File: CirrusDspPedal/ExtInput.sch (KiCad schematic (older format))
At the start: 8 parts, among them J5 MonoJack2Switch, SW1 P26L-1D-RND MTL, SW2 P26L-1D-RND MTL, U6 MCP601-xOT

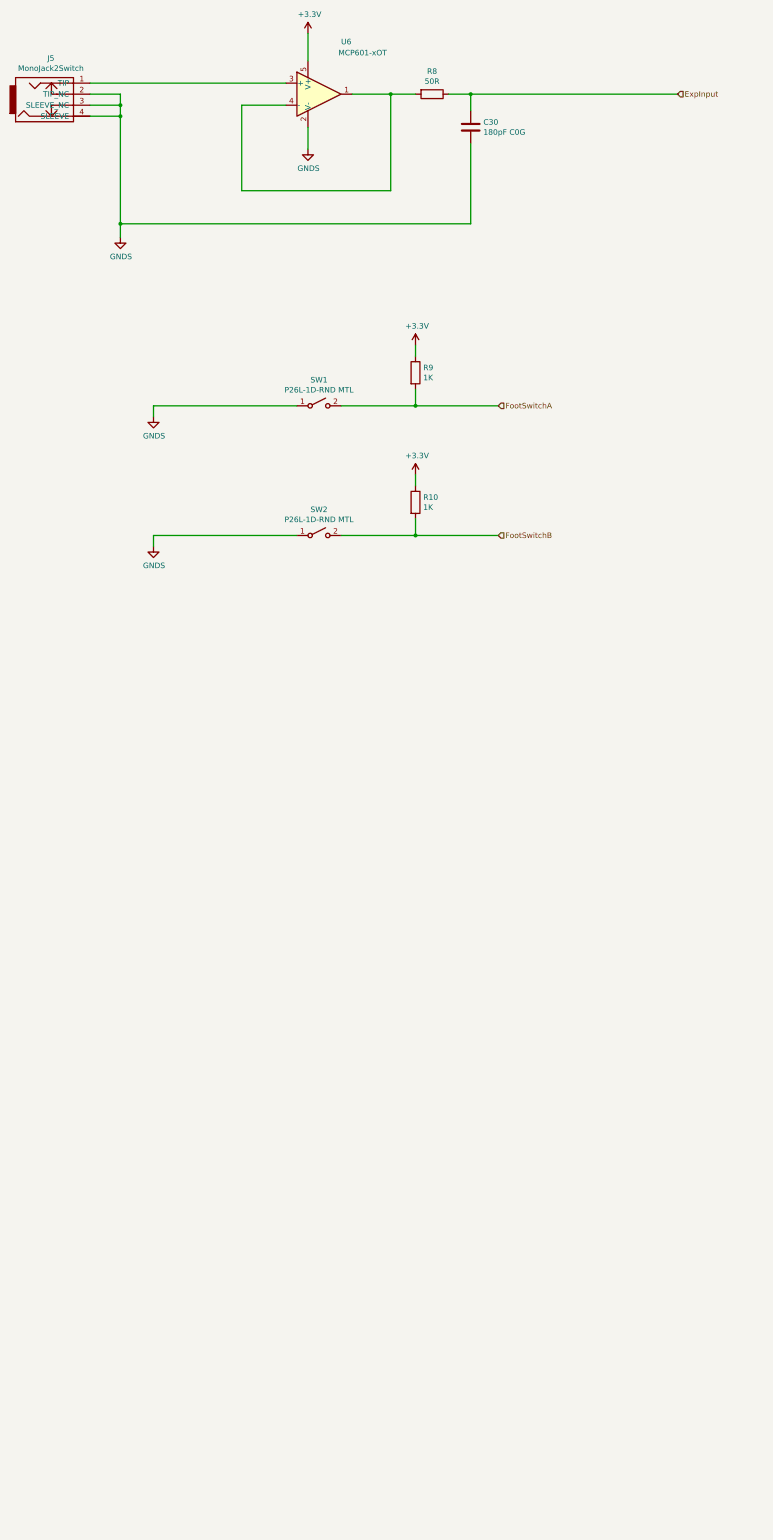
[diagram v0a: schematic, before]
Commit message: Added UserPots and RGB LEDS
Updated schema docs
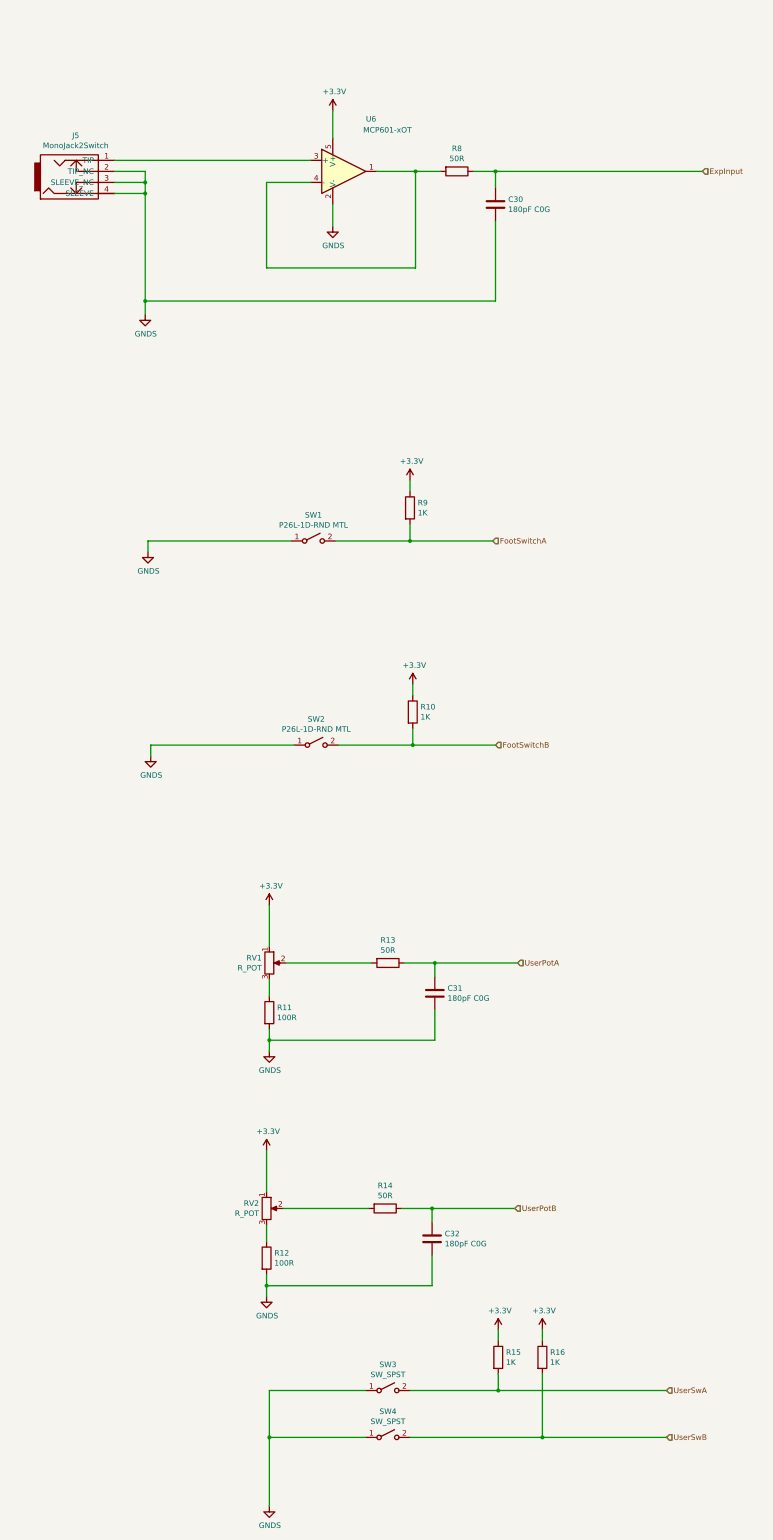
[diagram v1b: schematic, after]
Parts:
- added C31, C32: 180pF C0G, Capacitor_SMD:C_0805_2012Metric_Pad1.15x1.40mm_HandSolder, symbol Device:C
- added R11, R12: 100R, Resistor_SMD:R_0805_2012Metric_Pad1.15x1.40mm_HandSolder, symbol Device:R
- added R13, R14: 50R, Resistor_SMD:R_0805_2012Metric_Pad1.15x1.40mm_HandSolder, symbol Device:R
- added R15, R16: 1K, Resistor_SMD:R_0805_2012Metric_Pad1.15x1.40mm_HandSolder, symbol Device:R
- added RV1, RV2: R_POT, Potentiometer_THT:Potentiometer_Alps_RK09L_Single_Vertical, symbol Device:R_POT
- added SW3, SW4: SW_SPST, symbol Switch:SW_SPST
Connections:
- net +3V3: now also R15.1, R16.1, RV1.1, RV2.1
- net GNDS: now also C31.1, C32.1, R11.2, R12.2, SW3.1 (A), SW4.1 (A)
- new net: R13.2, RV1.2
- new net: R11.1, RV1.3
- new net: R14.2, RV2.2
- new net: R12.1, RV2.3
- new net UserPotA: C31.2, R13.1
- new net UserPotB: C32.2, R14.1
- new net UserSwA: R15.2, SW3.2 (B)
- new net UserSwB: R16.2, SW4.2 (B)
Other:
- moved on the sheet: C30, J5, R10, R8, R9, SW1, SW2, U6

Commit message: Completed schematic design
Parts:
- SW3, SW4: footprint (none) -> custom_sw:SW_SPDT_W6.86MM_L12.7MM_P4.8MM_D2MM
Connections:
- net ExpInput renamed FootExp_IN
- net FootSwitchA renamed FootSwitchA_IN
- net FootSwitchB renamed FootSwitchB_IN
- net UserPotA renamed UserPotA_IN
- net UserPotB renamed UserPotB_IN
- net UserSwA renamed UserSwitchA_IN
- net UserSwB renamed UserSwitchB_IN
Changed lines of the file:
@@
 $Descr A3 11693 16535 portrait
 encoding utf-8
-Sheet 9 10
+Sheet 10 11
 Title ""
 Date ""
@@
 $EndComp
 Text HLabel 8700 2400 2    50   Input ~ 0
-ExpInput
+FootExp_IN
 $Comp
 L Switch:SW_SPST SW1
@@
 	5375 5750 6050 5750
 Text HLabel 6800 5750 2    50   Input ~ 0
-FootSwitchA
+FootSwitchA_IN
 Wire Wire Line
 	6050 5750 6050 5600
@@
 	5400 7600 6075 7600
 Text HLabel 6825 7600 2    50   Input ~ 0
-FootSwitchB
+FootSwitchB_IN
 Wire Wire Line
 	6075 7600 6075 7450
@@
 	4925 9575 5700 9575
 Text HLabel 7025 9575 2    50   Input ~ 0
-UserPotA
+UserPotA_IN
 $Comp
 L Device:R R13
@@
 	4900 11800 5675 11800
 Text HLabel 7000 11800 2    50   Input ~ 0
-UserPotB
+UserPotB_IN
 $Comp
 L Device:R R14
@@
 F 0 "SW3" H 5850 13685 50  0000 C CNN
 F 1 "SW_SPST" H 5850 13594 50  0000 C CNN
-F 2 "" H 5850 13450 50  0001 C CNN
+F 2 "custom_sw:SW_SPDT_W6.86MM_L12.7MM_P4.8MM_D2MM" H 5850 13450 50  0001 C CNN
 F 3 "~" H 5850 13450 50  0001 C CNN
 	1    5850 13450
@@
 F 0 "SW4" H 5850 14110 50  0000 C CNN
 F 1 "SW_SPST" H 5850 14019 50  0000 C CNN
-F 2 "" H 5850 13875 50  0001 C CNN
+F 2 "custom_sw:SW_SPDT_W6.86MM_L12.7MM_P4.8MM_D2MM" H 5850 13875 50  0001 C CNN
 F 3 "~" H 5850 13875 50  0001 C CNN
 	1    5850 13875
@@
 $EndComp
 Text HLabel 8375 13450 2    50   Input ~ 0
-UserSwA
+UserSwitchA_IN
 Text HLabel 8375 13875 2    50   Input ~ 0
-UserSwB
+UserSwitchB_IN
 $EndSCHEMATC

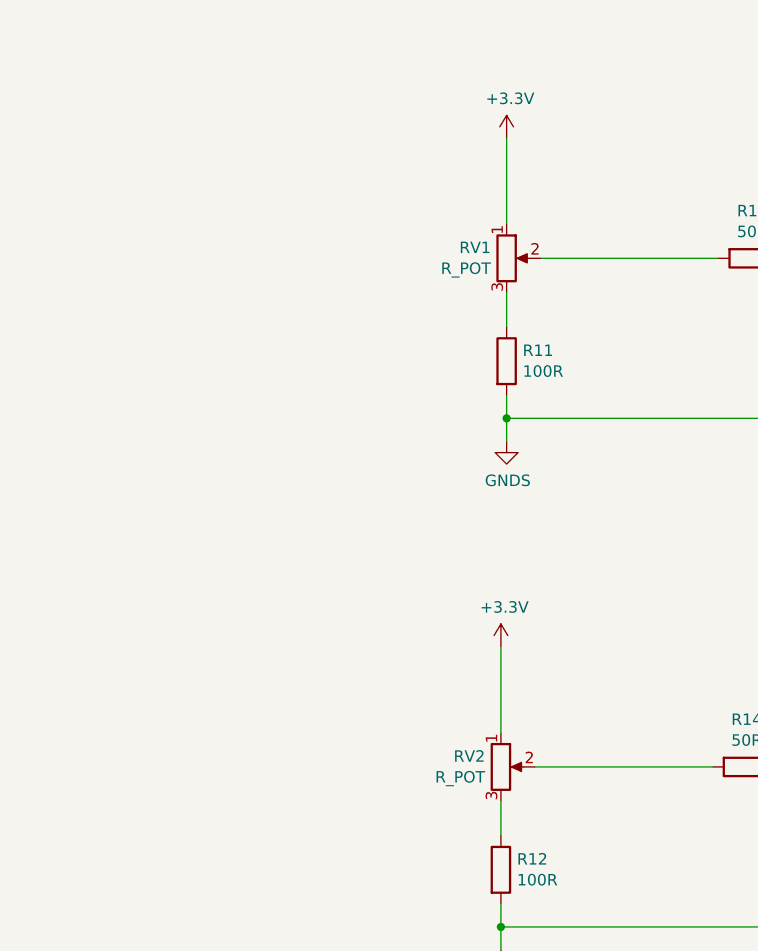
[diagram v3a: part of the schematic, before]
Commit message: finished RevA layout
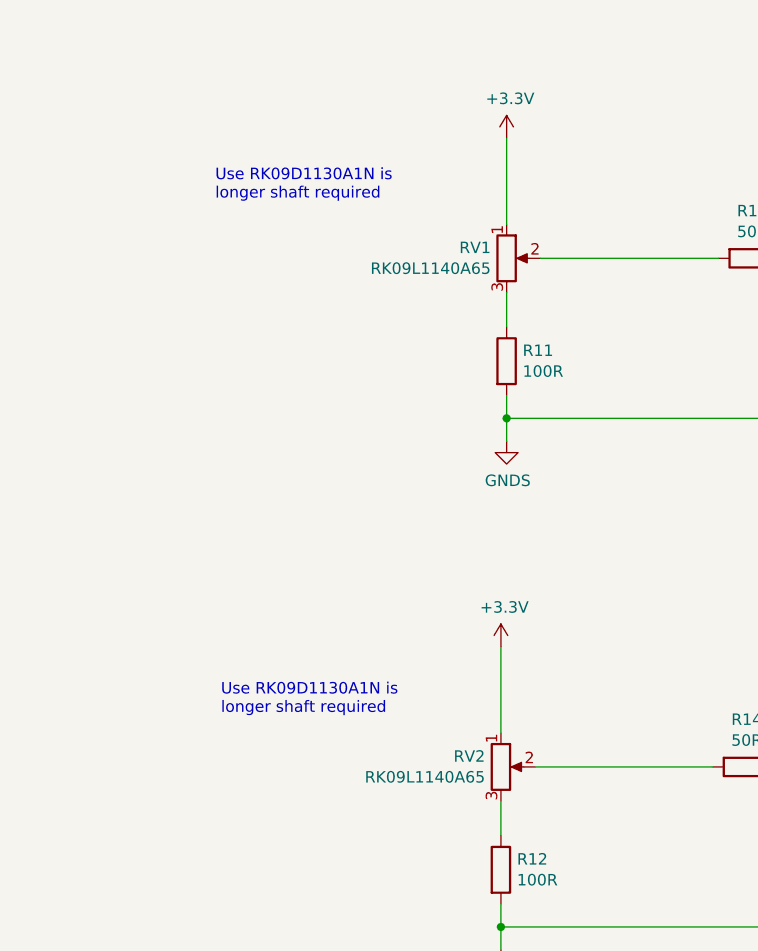
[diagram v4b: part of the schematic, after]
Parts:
- RV1, RV2: value R_POT -> RK09L1140A65
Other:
- note added: "Use RK09D1130A1N is \nlonger shaft required"
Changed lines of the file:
@@
 $Descr A3 11693 16535 portrait
 encoding utf-8
-Sheet 10 10
+Sheet 9 10
 Title ""
 Date ""
@@
 P 4775 9575
 F 0 "RV1" H 4706 9621 50  0000 R CNN
-F 1 "R_POT" H 4706 9530 50  0000 R CNN
+F 1 " RK09L1140A65" H 4706 9530 50  0000 R CNN
 F 2 "Potentiometer_THT:Potentiometer_Alps_RK09L_Single_Vertical" H 4775 9575 50  0001 C CNN
 F 3 "https://tech.alpsalpine.com/prod/e/pdf/potentiometer/rotarypotentiometers/rk09l/rk09l.pdf" H 4775 9575 50  0001 C CNN
@@
 P 4750 11800
 F 0 "RV2" H 4681 11846 50  0000 R CNN
-F 1 "R_POT" H 4681 11755 50  0000 R CNN
+F 1 " RK09L1140A65" H 4681 11755 50  0000 R CNN
 F 2 "Potentiometer_THT:Potentiometer_Alps_RK09L_Single_Vertical" H 4750 11800 50  0001 C CNN
 F 3 "https://tech.alpsalpine.com/prod/e/pdf/potentiometer/rotarypotentiometers/rk09l/rk09l.pdf" H 4750 11800 50  0001 C CNN
@@
 Text HLabel 8375 13875 2    50   Input ~ 0
 UserSwitchB_IN
+Text Notes 3525 11575 0    50   ~ 0
+Use RK09D1130A1N is \nlonger shaft required
+Text Notes 3500 9325 0    50   ~ 0
+Use RK09D1130A1N is \nlonger shaft required
 $EndSCHEMATC

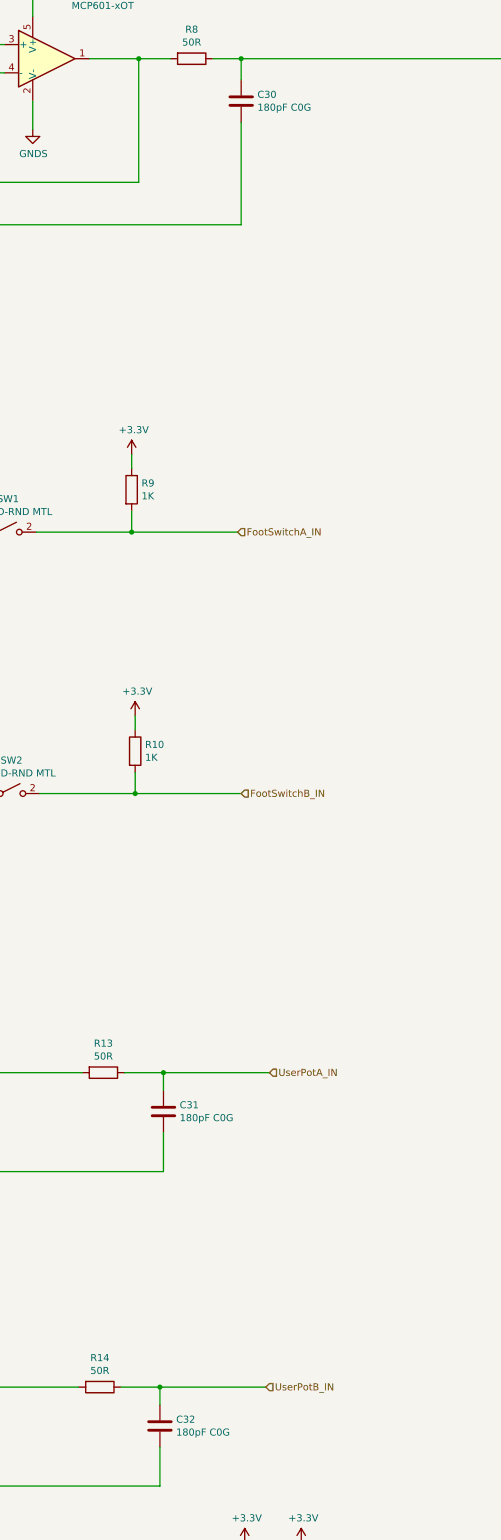
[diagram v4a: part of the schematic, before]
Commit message: replaced SDIO connector
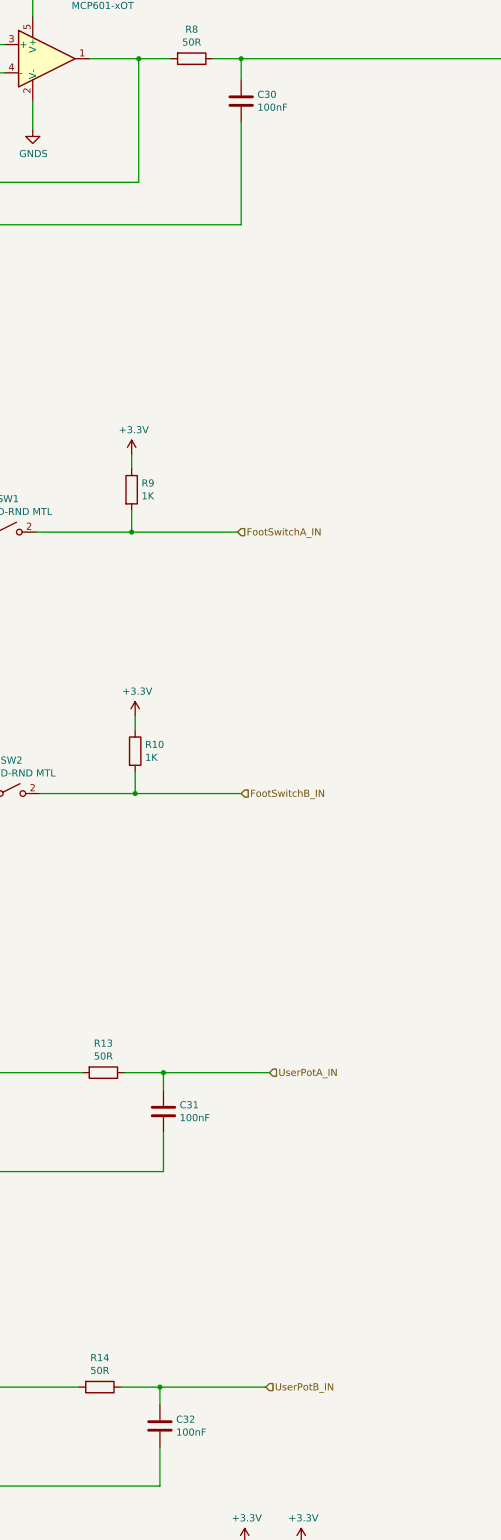
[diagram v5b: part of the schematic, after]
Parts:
- C30, C31, C32: value 180pF C0G -> 100nF
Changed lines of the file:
@@
 AR Path="/5F898CA5/5F89B764" Ref="C30"  Part="1"
 F 0 "C30" H 6710 2654 50  0000 R CNN
-F 1 "180pF C0G" H 6710 2745 50  0000 R CNN
+F 1 "100nF" H 6710 2745 50  0000 R CNN
 F 2 "Capacitor_SMD:C_0805_2012Metric_Pad1.15x1.40mm_HandSolder" H 6863 2550 50  0001 C CNN
 F 3 "~" H 6825 2700 50  0001 C CNN
@@
 AR Path="/5F898CA5/5F9025AC" Ref="C31"  Part="1"
 F 0 "C31" H 6160 9804 50  0000 R CNN
-F 1 "180pF C0G" H 6160 9895 50  0000 R CNN
+F 1 "100nF" H 6160 9895 50  0000 R CNN
 F 2 "Capacitor_SMD:C_0805_2012Metric_Pad1.15x1.40mm_HandSolder" H 6313 9700 50  0001 C CNN
 F 3 "~" H 6275 9850 50  0001 C CNN
@@
 AR Path="/5F898CA5/5F908FFE" Ref="C32"  Part="1"
 F 0 "C32" H 6135 12029 50  0000 R CNN
-F 1 "180pF C0G" H 6135 12120 50  0000 R CNN
+F 1 "100nF" H 6135 12120 50  0000 R CNN
 F 2 "Capacitor_SMD:C_0805_2012Metric_Pad1.15x1.40mm_HandSolder" H 6288 11925 50  0001 C CNN
 F 3 "~" H 6250 12075 50  0001 C CNN
